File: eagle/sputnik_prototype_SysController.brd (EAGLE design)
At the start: 99 x 100 mm, 61 parts, among them U1 MEGA128-A, X1 CRYSTAL-ABRACON-ABM3-SMD

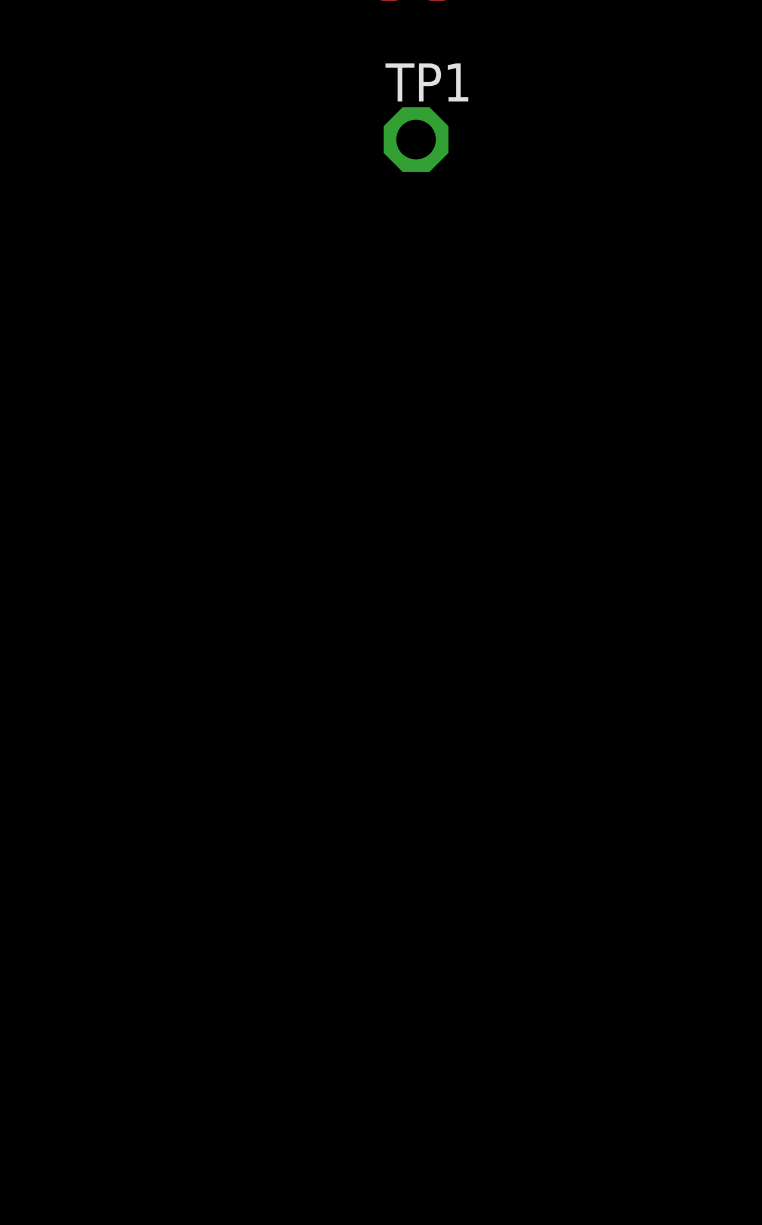
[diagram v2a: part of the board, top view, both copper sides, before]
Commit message: worked on the switch schematic
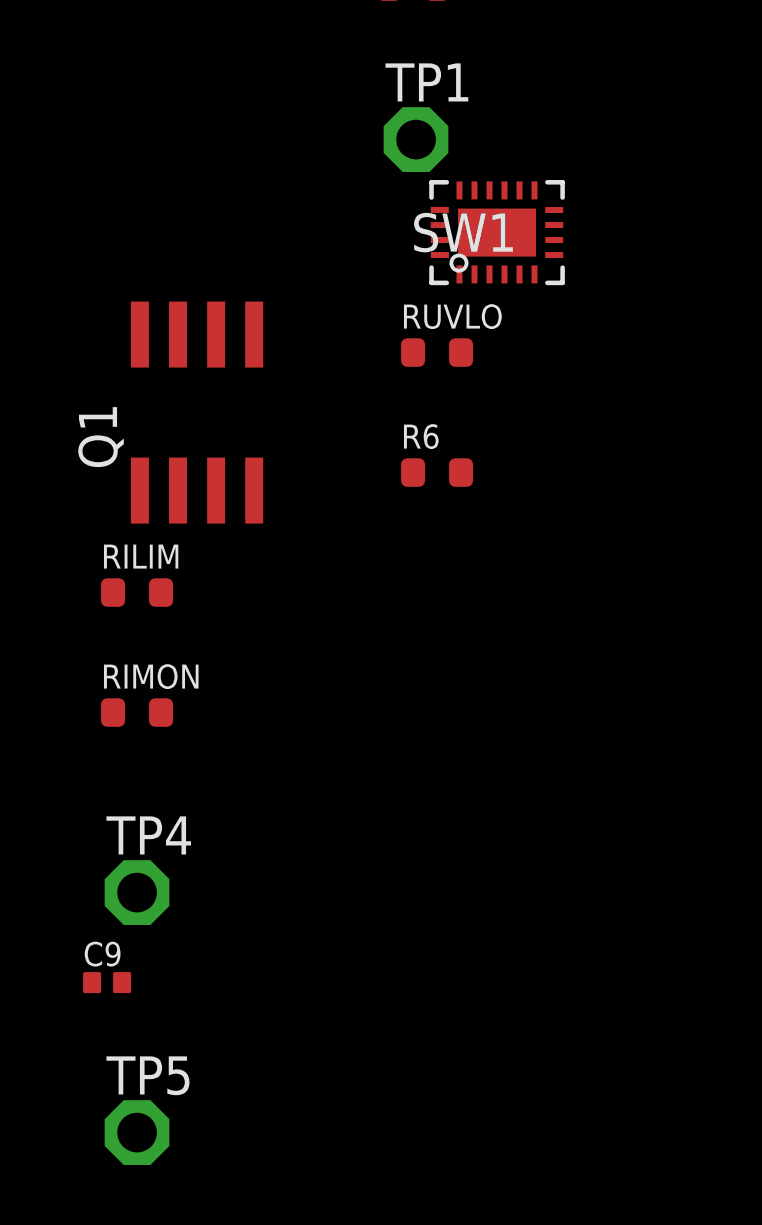
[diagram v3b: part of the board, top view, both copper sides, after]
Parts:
- added C9: 1uF, rcl_custom:.0402-B-NOSILK
- added Q1: (no value), transistor-power:SO-08
- added R6, RILIM, RIMON, RUVLO: Value, rcl_custom:.0603-B-NOSILK
- added SW1: TPS25944LRVCRWQFN-20-3X4, WQFN-20-3x4:QFN-20-L
- added TP4, TP5: TPSPAD1-13, testpad:P1-13
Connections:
- new net N$2: C9.1, RUVLO.1, SW1.10, SW1.11, SW1.12, SW1.13, SW1.9
- new net N$21: RILIM.1, SW1.17
- new net N$26: Q1.4
- new net N$27: RIMON.1, SW1.19, TP4.TP
- new net N$3: SW1.4, SW1.5, SW1.6, SW1.7, SW1.8
- new net N$7: SW1.20, TP5.TP
- new net N$9: Q1.5, Q1.6, Q1.7, Q1.8, R6.1, RUVLO.2, SW1.14
- net GND: now also C9.2, Q1.1, Q1.2, Q1.3, R6.2, RILIM.2, RIMON.2, SW1.1, SW1.15, SW1.16, SW1.18, SW1.2, SW1.21, SW1.3
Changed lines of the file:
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@@
 <?xml version="1.0" encoding="utf-8"?>
 <!DOCTYPE eagle SYSTEM "eagle.dtd">
-<eagle version="7.3.0">
+<eagle version="7.4.0">
 <drawing>
 <settings>
@@
 <element name="U$5" library="oresat-eagle" package="ORESAT-CARD-V0.3" value="" x="0" y="0" locked="yes"/>
 <element name="CF2" library="oresat-eagle" package="HARWIN-ARCHER-M50-3202045" value="ORESAT-CONNECTOR-40PIN" x="65.065" y="95.46" locked="yes"/>
+<element name="SW1" library="WQFN-20-3x4" package="QFN-20-L" value="TPS25944LRVCRWQFN-20-3X4" x="-67" y="-12"/>
+<element name="RUVLO" library="rcl_custom" package=".0603-B-NOSILK" value="Value" x="-69" y="-16"/>
+<element name="R6" library="rcl_custom" package=".0603-B-NOSILK" value="Value" x="-69" y="-20"/>
+<element name="Q1" library="transistor-power" package="SO-08" value="" x="-77" y="-18"/>
+<element name="RILIM" library="rcl_custom" package=".0603-B-NOSILK" value="Value" x="-79" y="-24"/>
+<element name="RIMON" library="rcl_custom" package=".0603-B-NOSILK" value="Value" x="-79" y="-28"/>
+<element name="TP4" library="testpad" package="P1-13" value="TPSPAD1-13" x="-79" y="-34">
+<attribute name="TP_SIGNAL_NAME" value="" x="-79" y="-34" size="1.778" layer="27" display="off"/>
+</element>
+<element name="C9" library="rcl_custom" package=".0402-B-NOSILK" value="1uF" x="-80" y="-37"/>
+<element name="TP5" library="testpad" package="P1-13" value="TPSPAD1-13" x="-79" y="-42">
+<attribute name="TP_SIGNAL_NAME" value="" x="-79" y="-42" size="1.778" layer="27" display="off"/>
+</element>
 </elements>
 <signals>
@@
 <vertex x="99" y="0"/>
 </polygon>
+<contactref element="SW1" pad="21"/>
+<contactref element="SW1" pad="16"/>
+<contactref element="SW1" pad="1"/>
+<contactref element="SW1" pad="15"/>
+<contactref element="SW1" pad="18"/>
+<contactref element="R6" pad="2"/>
+<contactref element="Q1" pad="2"/>
+<contactref element="Q1" pad="1"/>
+<contactref element="Q1" pad="3"/>
+<contactref element="RILIM" pad="2"/>
+<contactref element="SW1" pad="2"/>
+<contactref element="RIMON" pad="2"/>
+<contactref element="C9" pad="2"/>
+<contactref element="SW1" pad="3"/>
+<wire x1="19.27" y1="98" x2="18" y2="98" width="0" layer="19" extent="1-1"/>
+<wire x1="18" y1="92.92" x2="18" y2="98" width="0" layer="19" extent="1-1"/>
+<wire x1="19.27" y1="92.92" x2="18" y2="92.92" width="0" layer="19" extent="1-1"/>
+<wire x1="28.205" y1="76.28" x2="19.27" y2="92.92" width="0" layer="19" extent="1-1"/>
+<wire x1="9.95" y1="75.21" x2="28.205" y2="76.28" width="0" layer="19" extent="1-1"/>
+<wire x1="47.21" y1="59.59" x2="28.205" y2="76.28" width="0" layer="19" extent="1-1"/>
+<wire x1="55.21" y1="59.59" x2="47.21" y2="59.59" width="0" layer="19" extent="1-1"/>
+<wire x1="50.41" y1="43.99" x2="47.21" y2="59.59" width="0" layer="19" extent="1-1"/>
+<wire x1="-16.04" y1="71.12" x2="9.95" y2="75.21" width="0" layer="19" extent="1-1"/>
 <wire x1="-21.12" y1="71.12" x2="-16.04" y2="71.12" width="0" layer="19" extent="1-1"/>
 <wire x1="-24.93" y1="71.12" x2="-21.12" y2="71.12" width="0" layer="19" extent="1-1"/>
@@
 <wire x1="-63.03" y1="66.04" x2="-57.95" y2="66.04" width="0" layer="19" extent="1-1"/>
 <wire x1="-68.11" y1="66.04" x2="-63.03" y2="66.04" width="0" layer="19" extent="1-1"/>
-<wire x1="9.95" y1="75.21" x2="-16.04" y2="71.12" width="0" layer="19" extent="1-1"/>
 <wire x1="-62.85" y1="36.73" x2="-63.03" y2="66.04" width="0" layer="19" extent="1-1"/>
 <wire x1="-57.77" y1="36.73" x2="-62.85" y2="36.73" width="0" layer="19" extent="1-1"/>
@@
 <wire x1="-57.77" y1="30" x2="-62.85" y2="30" width="0" layer="19" extent="1-1"/>
 <wire x1="-47.61" y1="30" x2="-47.61" y2="36.73" width="0" layer="19" extent="1-1"/>
+<wire x1="49.01" y1="4.35" x2="50.41" y2="43.99" width="0" layer="19" extent="1-1"/>
+<wire x1="38.85" y1="4.35" x2="49.01" y2="4.35" width="0" layer="19" extent="1-1"/>
+<wire x1="-67.752" y1="-10.5945" x2="-62.85" y2="30" width="0" layer="19" extent="1-1"/>
+<wire x1="-68.252" y1="-10.5945" x2="-67.752" y2="-10.5945" width="0" layer="19" extent="1-1"/>
+<wire x1="-68.91" y1="-11.75" x2="-68.252" y2="-10.5945" width="0" layer="19" extent="1-1"/>
+<wire x1="-67" y1="-12" x2="-67.752" y2="-10.5945" width="0" layer="19" extent="1-1"/>
+<wire x1="-67.252" y1="-13.3945" x2="-67" y2="-12" width="0" layer="19" extent="1-1"/>
+<wire x1="-67.752" y1="-13.3945" x2="-67.252" y2="-13.3945" width="0" layer="19" extent="1-1"/>
+<wire x1="-68.252" y1="-13.3945" x2="-67.752" y2="-13.3945" width="0" layer="19" extent="1-1"/>
+<wire x1="-68.2" y1="-20" x2="-67.752" y2="-13.3945" width="0" layer="19" extent="1-1"/>
+<wire x1="-76.365" y1="-20.6" x2="-68.2" y2="-20" width="0" layer="19" extent="1-1"/>
+<wire x1="-77.635" y1="-20.6" x2="-76.365" y2="-20.6" width="0" layer="19" extent="1-1"/>
+<wire x1="-78.905" y1="-20.6" x2="-77.635" y2="-20.6" width="0" layer="19" extent="1-1"/>
+<wire x1="-78.2" y1="-24" x2="-77.635" y2="-20.6" width="0" layer="19" extent="1-1"/>
+<wire x1="-78.2" y1="-28" x2="-78.2" y2="-24" width="0" layer="19" extent="1-1"/>
+<wire x1="-79.5" y1="-37" x2="-78.2" y2="-28" width="0" layer="19" extent="1-1"/>
 </signal>
 <signal name="V+">
@@
 <wire x1="-50.15" y1="36.73" x2="-14.44" y2="71.12" width="0" layer="19" extent="1-1"/>
 </signal>
+<signal name="N$2">
+<contactref element="SW1" pad="9"/>
+<contactref element="SW1" pad="10"/>
+<contactref element="SW1" pad="12"/>
+<contactref element="SW1" pad="11"/>
+<contactref element="SW1" pad="13"/>
+<contactref element="RUVLO" pad="1"/>
+<contactref element="C9" pad="1"/>
+<wire x1="-69.8" y1="-16" x2="-80.5" y2="-37" width="0" layer="19" extent="1-1"/>
+<wire x1="-66.752" y1="-10.5945" x2="-69.8" y2="-16" width="0" layer="19" extent="1-1"/>
+<wire x1="-66.252" y1="-10.5945" x2="-66.752" y2="-10.5945" width="0" layer="19" extent="1-1"/>
+<wire x1="-65.752" y1="-10.5945" x2="-66.252" y2="-10.5945" width="0" layer="19" extent="1-1"/>
+<wire x1="-65.0945" y1="-11.248" x2="-65.752" y2="-10.5945" width="0" layer="19" extent="1-1"/>
+<wire x1="-65.0945" y1="-11.748" x2="-65.0945" y2="-11.248" width="0" layer="19" extent="1-1"/>
+</signal>
+<signal name="N$3">
+<contactref element="SW1" pad="7"/>
+<contactref element="SW1" pad="8"/>
+<contactref element="SW1" pad="5"/>
+<contactref element="SW1" pad="6"/>
+<contactref element="SW1" pad="4"/>
+<wire x1="-66.752" y1="-13.3945" x2="-66.252" y2="-13.3945" width="0" layer="19" extent="1-1"/>
+<wire x1="-65.752" y1="-13.3945" x2="-66.252" y2="-13.3945" width="0" layer="19" extent="1-1"/>
+<wire x1="-65.0945" y1="-12.748" x2="-65.752" y2="-13.3945" width="0" layer="19" extent="1-1"/>
+<wire x1="-65.0945" y1="-12.248" x2="-65.0945" y2="-12.748" width="0" layer="19" extent="1-1"/>
+</signal>
+<signal name="N$7">
+<contactref element="SW1" pad="20"/>
+<contactref element="TP5" pad="TP"/>
+<wire x1="-68.9045" y1="-12.748" x2="-79" y2="-42" width="0" layer="19" extent="1-1"/>
+</signal>
+<signal name="N$9">
+<contactref element="SW1" pad="14"/>
+<contactref element="RUVLO" pad="2"/>
+<contactref element="R6" pad="1"/>
+<contactref element="Q1" pad="8"/>
+<contactref element="Q1" pad="7"/>
+<contactref element="Q1" pad="6"/>
+<contactref element="Q1" pad="5"/>
+<wire x1="-77.635" y1="-15.4" x2="-78.905" y2="-15.4" width="0" layer="19" extent="1-1"/>
+<wire x1="-76.365" y1="-15.4" x2="-77.635" y2="-15.4" width="0" layer="19" extent="1-1"/>
+<wire x1="-75.095" y1="-15.4" x2="-76.365" y2="-15.4" width="0" layer="19" extent="1-1"/>
+<wire x1="-68.2" y1="-16" x2="-75.095" y2="-15.4" width="0" layer="19" extent="1-1"/>
+<wire x1="-69.8" y1="-20" x2="-68.2" y2="-16" width="0" layer="19" extent="1-1"/>
+<wire x1="-67.252" y1="-10.5945" x2="-68.2" y2="-16" width="0" layer="19" extent="1-1"/>
+</signal>
+<signal name="N$26">
+<contactref element="Q1" pad="4"/>
+</signal>
+<signal name="N$21">
+<contactref element="SW1" pad="17"/>
+<contactref element="RILIM" pad="1"/>
+<wire x1="-68.908" y1="-11.2445" x2="-79.8" y2="-24" width="0" layer="19" extent="1-1"/>
+</signal>
+<signal name="N$27">
+<contactref element="SW1" pad="19"/>
+<contactref element="RIMON" pad="1"/>
+<contactref element="TP4" pad="TP"/>
+<wire x1="-79.8" y1="-28" x2="-79" y2="-34" width="0" layer="19" extent="1-1"/>
+<wire x1="-68.9045" y1="-12.248" x2="-79.8" y2="-28" width="0" layer="19" extent="1-1"/>
+</signal>
 </signals>

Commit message: A few more changes
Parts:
- removed TP4, TP5: TPSPAD1-13, testpad:P1-13
- added C10: Value, rcl_custom:.0402-B-NOSILK
- added TP28, TP29: TPSPAD1-13, testpad:P1-13
- Q1: device transistor-power:SO-08 -> adafruit:SOT23
- moved Q1 60.0 mm to (-78.0, -78.0)
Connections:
- removed net N$7: SW1.20, TP5.TP
- new net N$25: SW1.2, TP29.TP
- new net N$28: SW1.3, TP28.TP
- new net N$29: SW1.20
- new net N$31: C10.1, SW1.18
- net GND: now also C10.2; no longer Q1.1, Q1.3, SW1.18, SW1.2, SW1.3
- net N$26: now also Q1.1; no longer Q1.4
- net N$27: no longer TP4.TP
- net N$9: now also Q1.3; no longer Q1.5, Q1.6, Q1.7, Q1.8

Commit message: latest changes
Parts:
- Q1: value (none) -> IRLML6344TRPBF
- moved Q1 7.00 mm to (-78.0, -71.0)
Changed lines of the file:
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@@
 </element>
 <element name="C10" library="rcl_custom" package=".0402-B-NOSILK" value="Value" x="-80" y="-65"/>
-<element name="Q1" library="adafruit" package="SOT23" value="" x="-78" y="-78"/>
+<element name="Q1" library="adafruit" package="SOT23" value="IRLML6344TRPBF" x="-78" y="-71"/>
 </elements>
 <signals>
@@
 <contactref element="SW1" pad="1"/>
 <contactref element="SW1" pad="15"/>
-<contactref element="R6" pad="2"/>
 <contactref element="RILIM" pad="2"/>
 <contactref element="RIMON" pad="2"/>
 <contactref element="C9" pad="2"/>
 <contactref element="C10" pad="2"/>
+<contactref element="R6" pad="2"/>
 <contactref element="Q1" pad="2"/>
-<wire x1="-79.5" y1="-65" x2="-77.05" y2="-79.1" width="0" layer="19" extent="1-1"/>
+<wire x1="-79.5" y1="-65" x2="-77.05" y2="-72.1" width="0" layer="19" extent="1-1"/>
 <wire x1="-79.5" y1="-37" x2="-79.5" y2="-65" width="0" layer="19" extent="1-1"/>
 <wire x1="-78.2" y1="-28" x2="-79.5" y2="-37" width="0" layer="19" extent="1-1"/>
@@
 <contactref element="R6" pad="1"/>
 <contactref element="Q1" pad="3"/>
-<wire x1="-69.8" y1="-20" x2="-78" y2="-76.9" width="0" layer="19" extent="1-1"/>
+<wire x1="-69.8" y1="-20" x2="-78" y2="-69.9" width="0" layer="19" extent="1-1"/>
 <wire x1="-68.2" y1="-16" x2="-69.8" y2="-20" width="0" layer="19" extent="1-1"/>
 <wire x1="-67.252" y1="-10.5945" x2="-68.2" y2="-16" width="0" layer="19" extent="1-1"/>

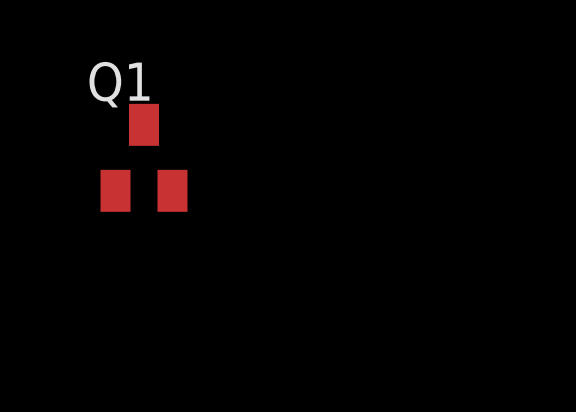
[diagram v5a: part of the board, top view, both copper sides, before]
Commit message: added a pull up resistor to FLT
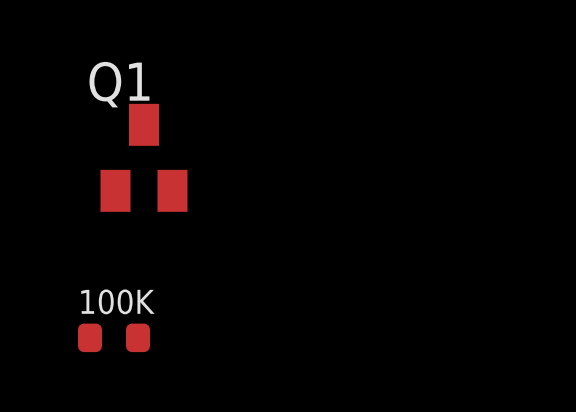
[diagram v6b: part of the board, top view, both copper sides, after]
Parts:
- added 100K: Value, rcl_custom:.0603-B-NOSILK
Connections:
- net N$2: now also 100K.1
- net N$29: now also 100K.2
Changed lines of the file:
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@@
 <element name="C10" library="rcl_custom" package=".0402-B-NOSILK" value="Value" x="-80" y="-65"/>
 <element name="Q1" library="adafruit" package="SOT23" value="IRLML6344TRPBF" x="-78" y="-71"/>
+<element name="100K" library="rcl_custom" package=".0603-B-NOSILK" value="Value" x="-79" y="-77"/>
 </elements>
 <signals>
@@
 <contactref element="RUVLO" pad="1"/>
 <contactref element="C9" pad="1"/>
+<contactref element="100K" pad="1"/>
+<wire x1="-80.5" y1="-37" x2="-79.8" y2="-77" width="0" layer="19" extent="1-1"/>
 <wire x1="-69.8" y1="-16" x2="-80.5" y2="-37" width="0" layer="19" extent="1-1"/>
 <wire x1="-66.752" y1="-10.5945" x2="-69.8" y2="-16" width="0" layer="19" extent="1-1"/>
@@
 <wire x1="-67.252" y1="-13.3945" x2="-79" y2="-47" width="0" layer="19" extent="1-1"/>
 </signal>
-<signal name="N$29">
-<contactref element="SW1" pad="20"/>
-</signal>
 <signal name="N$31">
 <contactref element="C10" pad="1"/>
@@
 <contactref element="Q1" pad="1"/>
 </signal>
+<signal name="N$29">
+<contactref element="100K" pad="2"/>
+<contactref element="SW1" pad="20"/>
+<wire x1="-68.9045" y1="-12.748" x2="-78.2" y2="-77" width="0" layer="19" extent="1-1"/>
+</signal>
 </signals>

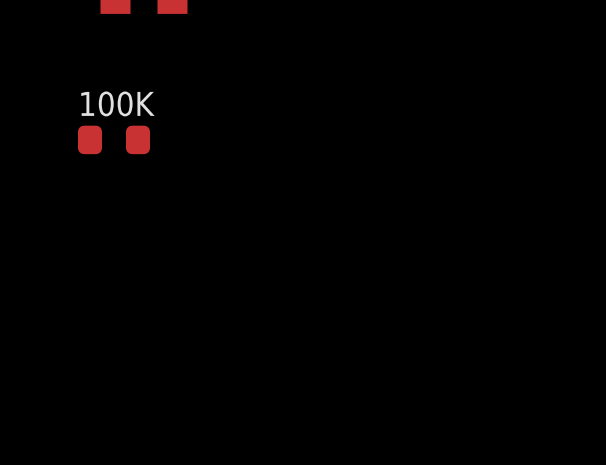
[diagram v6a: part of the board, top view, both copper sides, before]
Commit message: added the mux to the schematic
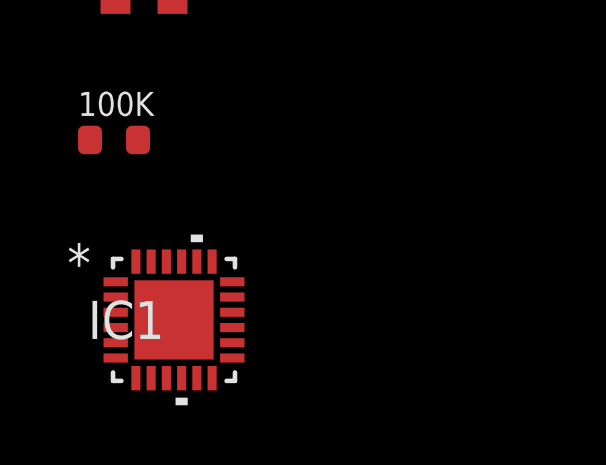
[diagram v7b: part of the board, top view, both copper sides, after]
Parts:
- added IC1: 74HC0467, QFN-24:QFN-24
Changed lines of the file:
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@@
 <element name="Q1" library="adafruit" package="SOT23" value="IRLML6344TRPBF" x="-78" y="-71"/>
 <element name="100K" library="rcl_custom" package=".0603-B-NOSILK" value="Value" x="-79" y="-77"/>
+<element name="IC1" library="QFN-24" package="QFN-24" value="74HC0467" x="-77" y="-83"/>
 </elements>
 <signals>

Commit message: added the updated mux to the schematic
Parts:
- IC1: value 74HC0467 -> 74HC4067
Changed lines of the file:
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@@
 <element name="Q1" library="adafruit" package="SOT23" value="IRLML6344TRPBF" x="-78" y="-71"/>
 <element name="100K" library="rcl_custom" package=".0603-B-NOSILK" value="Value" x="-79" y="-77"/>
-<element name="IC1" library="QFN-24" package="QFN-24" value="74HC0467" x="-77" y="-83"/>
+<element name="IC1" library="QFN-24" package="QFN-24" value="74HC4067" x="-77" y="-83"/>
 </elements>
 <signals>
